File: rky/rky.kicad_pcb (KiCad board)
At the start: 2 copper layers, 51 parts, among them J1 UART, J3 Li-Ion 3.7 CONN, J4 USB_C_Receptacle_USB2.0, J5 EXTRA, SW1 SW_SPDT, U1 ESP8266-12E/ESP-12E, U3 ATmega328PB-A, U4 LM3940IMP-3.3/NOPB, U6 SSD1306, Y1 16MHZ

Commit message: rough pcb layout create
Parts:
- removed the C12 at (133.3, 106.0)
- removed the C13 at (156.1, 86.5)
- removed C14: 10p, Capacitor_SMD:C_0603_1608Metric
- removed J5: EXTRA, TEST_POINT_MATRIX_6-PIN:6PIN_CONN
- removed the R11 at (129.3, 108.5)
- removed TP1: AT_RST#, TestPoint:TestPoint_Pad_D1.0mm
- removed the U3 at (140.6, 80.3)
- removed Y1: 16MHZ, Crystal:Crystal_SMD_0603-2Pin_6.0x3.5mm
- added U6: NRF24L01, Package_DFN_QFN:QFN-20-1EP_4x4mm_P0.5mm_EP2.5x2.5mm, B.Cu at (118.9, 94.5)
- B_TEMP1, C1, C2, D-1, D3, SW1, U4: moved to B.Cu
- C13: renamed from C24; moved to B.Cu
- C4: renamed from C8; moved to B.Cu
- C5: renamed from C4; moved to B.Cu
- C6: renamed from C5; moved to B.Cu
- C7: renamed from C6; moved to B.Cu
- C8: renamed from C7; moved to B.Cu
- J3: renamed from J4; moved to B.Cu
- JP2: renamed from JP8; moved to B.Cu
- JP3: renamed from JP2; moved to B.Cu
- R10: renamed from R26; moved to B.Cu
- R2: renamed from R3; moved to B.Cu
- R3: renamed from R6; moved to B.Cu
- R4: renamed from R7; moved to B.Cu
- R5: renamed from R4; moved to B.Cu
- R9: renamed from R25; moved to B.Cu
- U2: renamed from U6; moved to B.Cu
- moved C12 58.9 mm to (106.7, 77.2), turned to 90 degrees
- moved C5 53.8 mm to (112.8, 83.6)
- moved C10 51.1 mm to (111.0, 83.1), turned to 90 degrees
- moved D-1 50.1 mm to (112.3, 76.5), turned to 180 degrees
- moved R9 47.1 mm to (121.4, 101.6), turned to 90 degrees
- moved R11 45.4 mm to (113.0, 78.6), turned to -90 degrees
- moved C6 45.3 mm to (103.6, 79.8), turned to 180 degrees
- moved J2 44.7 mm to (104.0, 76.2), turned to 180 degrees
- moved R4 44.3 mm to (118.1, 83.8), turned to -90 degrees
- moved U4 44.1 mm to (119.1, 108.7), turned to -90 degrees
- moved R8 41.0 mm to (115.3, 74.4), turned to -90 degrees
- moved R6 38.4 mm to (108.5, 84.1)
- moved B_TEMP1 37.6 mm to (111.5, 89.7), turned to 180 degrees
- moved R5 37.2 mm to (111.8, 94.0), turned to 180 degrees
- moved JP1 34.7 mm to (123.9, 76.0)
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- renumbered C21 to C10, C22 to C11, C23 to C12, C20 to C9, J3 to J2, R27 to R11, R22 to R6, R23 to R7, R24 to R8, U1 to U3
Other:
- board outline added: 24.9 x 41.1 mm

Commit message: schematic update
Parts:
- added C14: 4.7uf, Capacitor_SMD:C_0603_1608Metric, F.Cu at (108.6, 106.7)
- added DRIVE1: PTS525SM15SMTR2LFS, push button:SW_PTS525SM15SMTR2LFS, F.Cu at (132.1, 101.0)
- added DRIVE2: PTS525SM15SMTR2LFS, push button:SW_PTS525SM15SMTR2LFS, F.Cu at (122.6, 76.8)
- added R12: 10k, Resistor_SMD:R_0603_1608Metric, F.Cu at (112.6, 106.7)
- added SELECT1: PTS525SM15SMTR2LFS, push button:SW_PTS525SM15SMTR2LFS, F.Cu at (141.6, 94.3)
- moved JP1 32.2 mm to (127.7, 108.0), turned to 90 degrees
- moved J1 22.2 mm to (125.0, 99.0)
- moved C3 18.8 mm to (103.5, 82.4)
- moved C4 4.70 mm to (124.7, 107.3)
- moved C1 4.45 mm to (119.4, 87.0)
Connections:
- C12 pad 2: GND -> Net-(C12-Pad2)
- C13 pad 2: GND -> Net-(C12-Pad2)

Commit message: remove cp2102
new layout
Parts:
- removed JP3: SolderJumper_3_Open, TEST_POINT_MATRIX_6-PIN:3_PIN_SOLDER_JUMPER_SMD
- removed RST_CP1: 0-RST, TestPoint:TestPoint_Pad_D1.0mm
- added C15: 2.2nf, Capacitor_SMD:C_0603_1608Metric_Pad1.08x0.95mm_HandSolder, F.Cu at (125.0, 98.6)
- added C16: 4.7pf, Capacitor_SMD:C_0603_1608Metric_Pad1.08x0.95mm_HandSolder, F.Cu at (124.0, 87.9)
- added C17: 22pf, Capacitor_SMD:C_0603_1608Metric_Pad1.08x0.95mm_HandSolder, F.Cu at (122.4, 82.8)
- added C18: 33nf, Capacitor_SMD:C_0603_1608Metric_Pad1.08x0.95mm_HandSolder, F.Cu at (104.1, 110.2)
- added C19: 22pf, Capacitor_SMD:C_0603_1608Metric_Pad1.08x0.95mm_HandSolder, B.Cu at (123.4, 78.7)
- added J4: Conn_01x04_Male, Connector_PinHeader_1.00mm:PinHeader_1x04_P1.00mm_Vertical, F.Cu at (103.6, 91.0)
- added J5: Conn_02x03_Odd_Even, Connector_PinHeader_1.27mm:PinHeader_2x03_P1.27mm_Vertical_SMD, B.Cu at (121.9, 85.1)
- added R13: 1M, Resistor_SMD:R_0603_1608Metric_Pad0.98x0.95mm_HandSolder, B.Cu at (121.9, 73.7)
- C1: value 4.7uf -> 1nf; footprint Capacitor_SMD:C_0603_1608Metric -> Capacitor_SMD:C_0603_1608Metric_Pad1.08x0.95mm_HandSolder; moved to F.Cu
- C2: value .1uf -> 10nf; footprint Capacitor_SMD:C_0603_1608Metric -> Capacitor_SMD:C_0603_1608Metric_Pad1.08x0.95mm_HandSolder
- C3: value 1uf -> 1.5pf; footprint Capacitor_SMD:C_0603_1608Metric -> Capacitor_SMD:C_0603_1608Metric_Pad1.08x0.95mm_HandSolder
- C4: value .1uf -> 1.0pf; footprint Capacitor_SMD:C_0603_1608Metric -> Capacitor_SMD:C_0603_1608Metric_Pad1.08x0.95mm_HandSolder; moved to F.Cu
- J1: value UART -> Conn_01x02_Male; footprint Connector_PinHeader_1.00mm:PinHeader_1x05_P1.00mm_Horizontal -> Connector_PinHeader_1.00mm:PinHeader_1x02_P1.00mm_Horizontal
- JP1: value SolderJumper_3_Open -> SolderJumper_2_Open; footprint TEST_POINT_MATRIX_6-PIN:3_PIN_SOLDER_JUMPER_SMD -> Jumper:SolderJumper-2_P1.3mm_Bridged2Bar_RoundedPad1.0x1.5mm
- JP2: value RST -> SolderJumper_2_Open; footprint TEST_POINT_MATRIX_6-PIN:2_PIN_SMD_SOLDER_JUMPER -> Jumper:SolderJumper-2_P1.3mm_Bridged2Bar_RoundedPad1.0x1.5mm; moved to F.Cu
- R1: value 4.7k -> 1k; footprint Resistor_SMD:R_0603_1608Metric -> Resistor_SMD:R_0603_1608Metric_Pad0.98x0.95mm_HandSolder
- R4: value 10k -> 22k; footprint Resistor_SMD:R_0603_1608Metric -> Resistor_SMD:R_0603_1608Metric_Pad0.98x0.95mm_HandSolder; moved to F.Cu
- SELECT1: moved to B.Cu
- moved C3 27.4 mm to (111.1, 108.7), turned to 0 degrees
- moved SELECT1 23.2 mm to (118.9, 99.1), turned to -90 degrees
- moved R1 22.9 mm to (103.6, 98.6), turned to 90 degrees
- moved J1 22.9 mm to (103.6, 107.2), turned to 180 degrees
- moved DRIVE1 16.0 mm to (118.4, 109.2)
- moved C4 12.9 mm to (112.3, 110.7), turned to 0 degrees
- moved R9 12.1 mm to (114.8, 91.4)
- moved C2 11.5 mm to (123.4, 76.2), turned to 180 degrees
- moved R3 7.47 mm to (111.3, 104.1)
- moved R4 6.19 mm to (124.0, 85.9), turned to 0 degrees
- moved JP2 5.77 mm to (125.0, 92.5), turned to 90 degrees
- moved C1 4.94 mm to (117.9, 82.3), turned to 0 degrees
- moved JP1 4.71 mm to (125.0, 104.1), turned to -90 degrees
- moved U6 3.05 mm to (118.9, 91.4)
- moved D1 1.88 mm to (120.4, 85.9)
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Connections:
- C1 pad 1: Net-(C1-Pad1) -> Net-(U6-Pad15)
- C2 pad 1: GND -> Net-(U6-Pad15)
- C2 pad 2: Net-(C1-Pad1) -> GND
- C3 pad 1: VIN -> Net-(C3-Pad1)
- C3 pad 2: GND -> /50ohm/RF-IO
- C4 pad 1: Net-(C4-Pad1) -> GND
- C4 pad 2: /RST# -> /50ohm/RF-IO
- DRIVE1 pad 3: unconnected-(DRIVE1-Pad3) -> Net-(DRIVE1-Pad3)
- DRIVE1 pad 4: unconnected-(DRIVE1-Pad4) -> GND
- J1 pad 1: VIN -> /RXD
- J1 pad 2: GND -> /TXD
- JP1 pad 1: /AT_RXD -> Net-(U3-Pad3)
- JP1 pad 2: Net-(J1-Pad3) -> GND
- JP2 pad 1: Net-(JP2-Pad1) -> /ce
- JP2 pad 2: Net-(C4-Pad1) -> GND
- R1 pad 1: VIN -> /ce
- R1 pad 2: Net-(R1-Pad2) -> Net-(U3-Pad17)
- R4 pad 1: Net-(R4-Pad1) -> Net-(U6-Pad16)
- SELECT1 pad 3: unconnected-(SELECT1-Pad3) -> GND
- SELECT1 pad 4: unconnected-(SELECT1-Pad4) -> Net-(SELECT1-Pad4)
- U3 pad 1: unconnected-(U3-Pad1) -> /reset
- U3 pad 10: unconnected-(U3-Pad10) -> /miso
- U3 pad 11: unconnected-(U3-Pad11) -> Net-(U3-Pad11)
- U3 pad 12: unconnected-(U3-Pad12) -> Net-(U3-Pad12)
- U3 pad 13: unconnected-(U3-Pad13) -> /mosi
- U3 pad 14: unconnected-(U3-Pad14) -> /sck
- U3 pad 15: unconnected-(U3-Pad15) -> GND
- U3 pad 16: unconnected-(U3-Pad16) -> Net-(DRIVE1-Pad3)
- U3 pad 17: unconnected-(U3-Pad17) -> Net-(U3-Pad17)
- U3 pad 18: unconnected-(U3-Pad18) -> /irq
- U3 pad 19: unconnected-(U3-Pad19) -> Net-(U3-Pad19)
- U3 pad 20: unconnected-(U3-Pad20) -> Net-(U3-Pad20)
- U3 pad 21: unconnected-(U3-Pad21) -> /RXD
- U3 pad 22: unconnected-(U3-Pad22) -> /TXD
- U3 pad 3: unconnected-(U3-Pad3) -> Net-(U3-Pad3)
- U3 pad 4: unconnected-(U3-Pad4) -> Net-(SELECT1-Pad4)
- U3 pad 8: unconnected-(U3-Pad8) -> +3V3
- U3 pad 9: unconnected-(U3-Pad9) -> /csn
- U6 pad 1: unconnected-(U6-Pad1) -> /ce
- U6 pad 10: unconnected-(U6-Pad10) -> Net-(U6-Pad10)
- U6 pad 11: unconnected-(U6-Pad11) -> Net-(U6-Pad11)
- U6 pad 12: unconnected-(U6-Pad12) -> Net-(U6-Pad12)
- U6 pad 13: unconnected-(U6-Pad13) -> Net-(U6-Pad13)
- U6 pad 14: unconnected-(U6-Pad14) -> GND
- U6 pad 15: unconnected-(U6-Pad15) -> Net-(U6-Pad15)
- U6 pad 16: unconnected-(U6-Pad16) -> Net-(U6-Pad16)
- U6 pad 17: unconnected-(U6-Pad17) -> GND
- U6 pad 18: unconnected-(U6-Pad18) -> Net-(U6-Pad15)
- U6 pad 19: unconnected-(U6-Pad19) -> Net-(U6-Pad19)
- U6 pad 2: unconnected-(U6-Pad2) -> /csn
- U6 pad 20: unconnected-(U6-Pad20) -> GND
- U6 pad 3: unconnected-(U6-Pad3) -> /sck
- U6 pad 4: unconnected-(U6-Pad4) -> /mosi
- U6 pad 5: unconnected-(U6-Pad5) -> /miso
- U6 pad 6: unconnected-(U6-Pad6) -> /irq
- U6 pad 7: unconnected-(U6-Pad7) -> Net-(U6-Pad15)
- U6 pad 8: unconnected-(U6-Pad8) -> GND
- U6 pad 9: unconnected-(U6-Pad9) -> Net-(U6-Pad9)

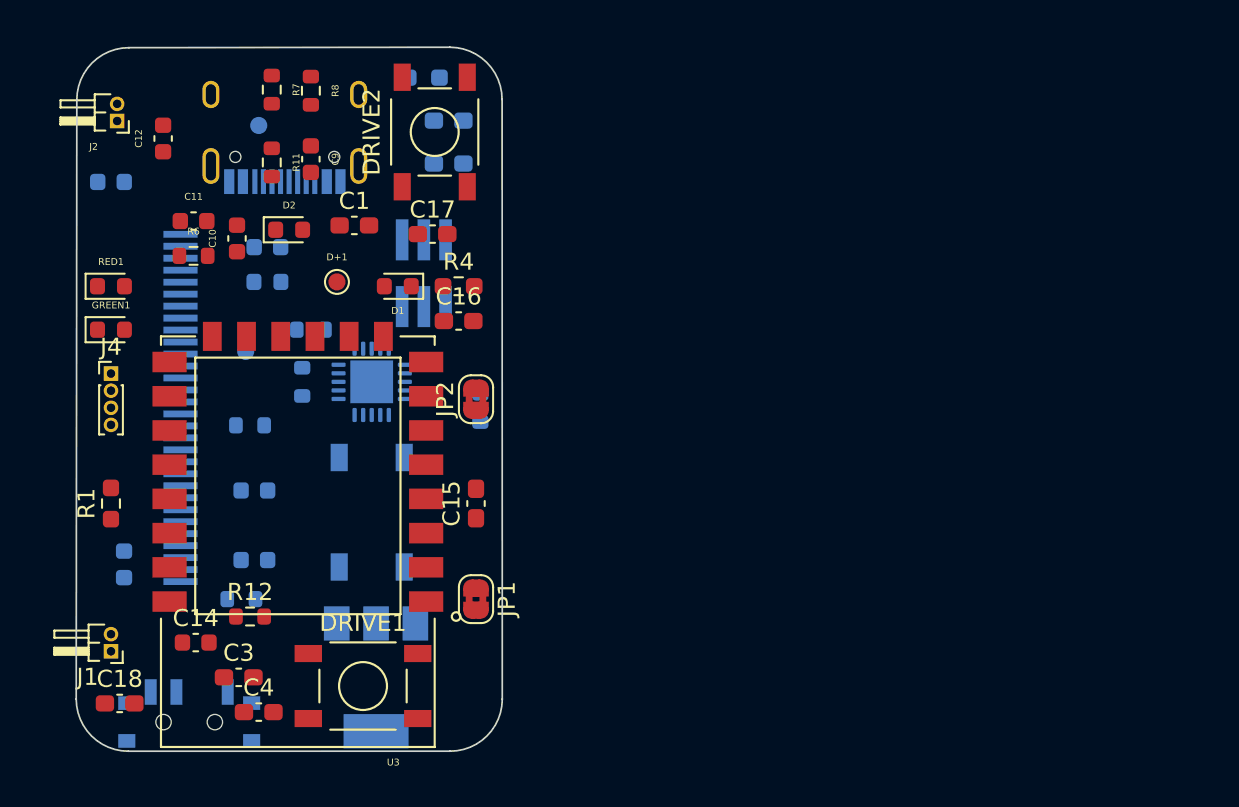
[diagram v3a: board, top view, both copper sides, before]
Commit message: component place
 first touch component placement complete
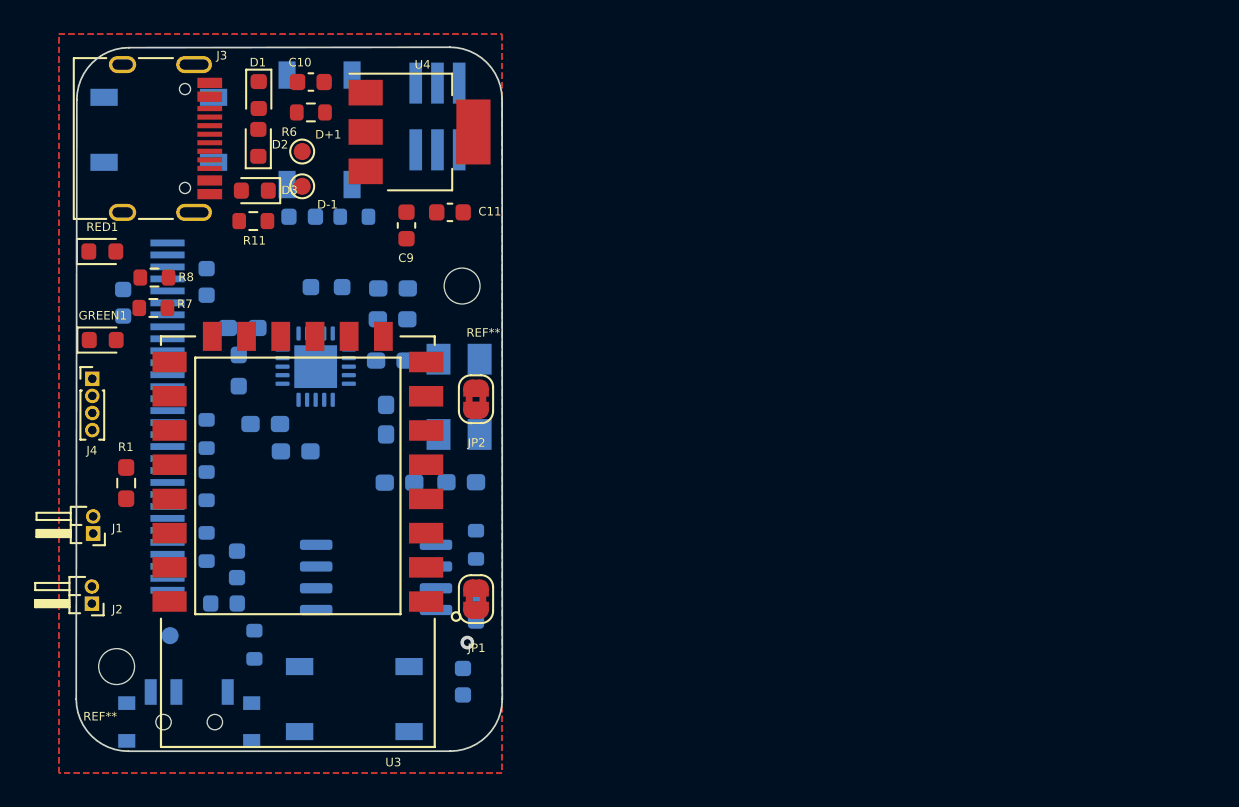
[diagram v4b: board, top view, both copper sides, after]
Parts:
- added REF**: MountingHole_2.1mm, MountingHole:MountingHole_2.1mm, F.Cu at (124.2, 85.8)
- added REF**: MountingHole_2.1mm, MountingHole:MountingHole_2.1mm, F.Cu at (104.0, 108.1)
- added U5: TP4056, Package_SO:SO-8_5.3x6.2mm_P1.27mm, B.Cu at (119.1, 102.9)
- added Y1: 16MHZ, Crystal:Crystal_SMD_0603-4Pin_6.0x3.5mm, B.Cu at (124.0, 92.3)
- C1, C12, C14, C15, C16, C17, C18, C3, C4, DRIVE1, DRIVE2, R12, R4: moved to B.Cu
- D-1, D3, J3, U4: moved to F.Cu
- moved C12 36.3 mm to (124.2, 109.0), turned to -90 degrees
- moved DRIVE1 32.6 mm to (115.8, 76.7), turned to 90 degrees
- moved U4 32.0 mm to (121.7, 76.8), turned to 0 degrees
- moved J2 28.3 mm to (102.5, 104.4)
- moved C14 25.7 mm to (114.8, 81.8)
- moved R12 24.2 mm to (117.9, 81.8)
- moved C18 22.7 mm to (119.7, 93.6), turned to -90 degrees
- moved C2 21.3 mm to (114.4, 95.5), turned to 0 degrees
- moved C13 20.7 mm to (125.0, 104.6)
- moved R13 20.3 mm to (111.1, 90.8), turned to -90 degrees
- moved C4 17.9 mm to (124.1, 97.3), turned to 180 degrees
- moved B_TEMP1 17.2 mm to (107.1, 106.3)
- moved DRIVE2 16.1 mm to (106.4, 76.7), turned to 0 degrees
- moved R9 15.6 mm to (112.0, 106.8), turned to -90 degrees
- moved C11 15.0 mm to (123.4, 81.5)
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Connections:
- J1 pad 1: /RXD -> /TXD
- J1 pad 2: /TXD -> /RXD
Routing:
- net GND: vias 0 -> 1
- added copper zone on B.Cu, net GND
- added copper zone on F.Cu, net GND
- added copper zone on F.Cu, net VCC

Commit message: add render folder
kicad 3d render image folder add
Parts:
- removed the REF** at (124.2, 85.8)
- removed the REF** at (104.0, 108.1)
- removed SW1: SW_SPDT, Button_Switch_SMD:SW_SPDT_PCM12
- added REF**: MountingHole_2.1mm, MountingHole:MountingHole_2.1mm, F.Cu at (124.0, 85.0)
- added REF**: MountingHole_2.1mm, MountingHole:MountingHole_2.1mm, F.Cu at (104.0, 110.0)
- added REF**: OSHW-Logo2_7.3x6mm_SilkScreen, Symbol:OSHW-Logo2_7.3x6mm_SilkScreen, B.Cu at (109.9, 109.9)
- J5: moved to F.Cu
- moved SELECT1 33.6 mm to (122.8, 76.7), turned to -90 degrees
- moved J5 10.5 mm to (116.0, 84.0), turned to 180 degrees
- moved R9 8.66 mm to (114.7, 98.6), turned to 0 degrees
- moved B_TEMP1 8.51 mm to (111.5, 99.0)
- moved D3 3.26 mm to (112.0, 77.0)
- moved D2 2.33 mm to (112.0, 79.8)
- moved D+1 2.03 mm to (115.0, 80.0)
- moved D-1 2.02 mm to (115.0, 78.0)
- moved R11 1.35 mm to (111.0, 83.0), turned to -90 degrees
- moved R1 1.04 mm to (103.5, 97.2)
- moved C2 1.02 mm to (114.3, 96.5)
- moved R5 0.99 mm to (109.9, 100.3)
- moved C7 0.92 mm to (111.8, 101.6)
- moved C8 0.25 mm to (110.2, 104.1)
- turned D1 to 90 degrees
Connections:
- net Net-(J4-Pad1) renamed /SDA
- net Net-(J4-Pad2) renamed /SCL
- C12 pad 1: /BATTERY +VE -> VCC
- J2 pad 1: /BATTERY +VE -> VCC
- U5 pad 5: /BATTERY +VE -> VCC
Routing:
- net Net-(GREEN1-Pad1): track 0.00 -> 28.9 mm, vias 0 -> 1
- net VCC: track 0.00 -> 24.5 mm, vias 0 -> 1
- net /reset: track 0.00 -> 24.0 mm
- net Net-(SELECT1-Pad4): track 0.00 -> 22.7 mm, vias 0 -> 1
- net +3V3: track 0.00 -> 21.1 mm
- net GND: track 0.00 -> 20.0 mm
- net Net-(DRIVE2-Pad1): track 0.00 -> 19.1 mm
- net /mosi: track 0.00 -> 17.8 mm, vias 0 -> 1
- net Net-(C13-Pad1): track 0.00 -> 16.1 mm
- net Net-(B_TEMP1-Pad1): track 0.00 -> 15.6 mm
- net 3.3V: track 0.00 -> 13.9 mm
- net Net-(R1-Pad2): track 0.00 -> 11.6 mm, vias 0 -> 2
- net /SCL: track 0.00 -> 10.4 mm
- net VIN: track 0.00 -> 10.2 mm
- net /sck: track 0.00 -> 9.73 mm, vias 0 -> 1
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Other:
- board text added: "Diginto.tech/blog/rky"
- board text added: "Rky Controller"
- board text added: "Version. 1.0"
